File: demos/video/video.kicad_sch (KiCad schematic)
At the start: 5 parts, among them J4 DB9FEM, P1 BNC, P2 BNC, P3 BNC, P8 BNC

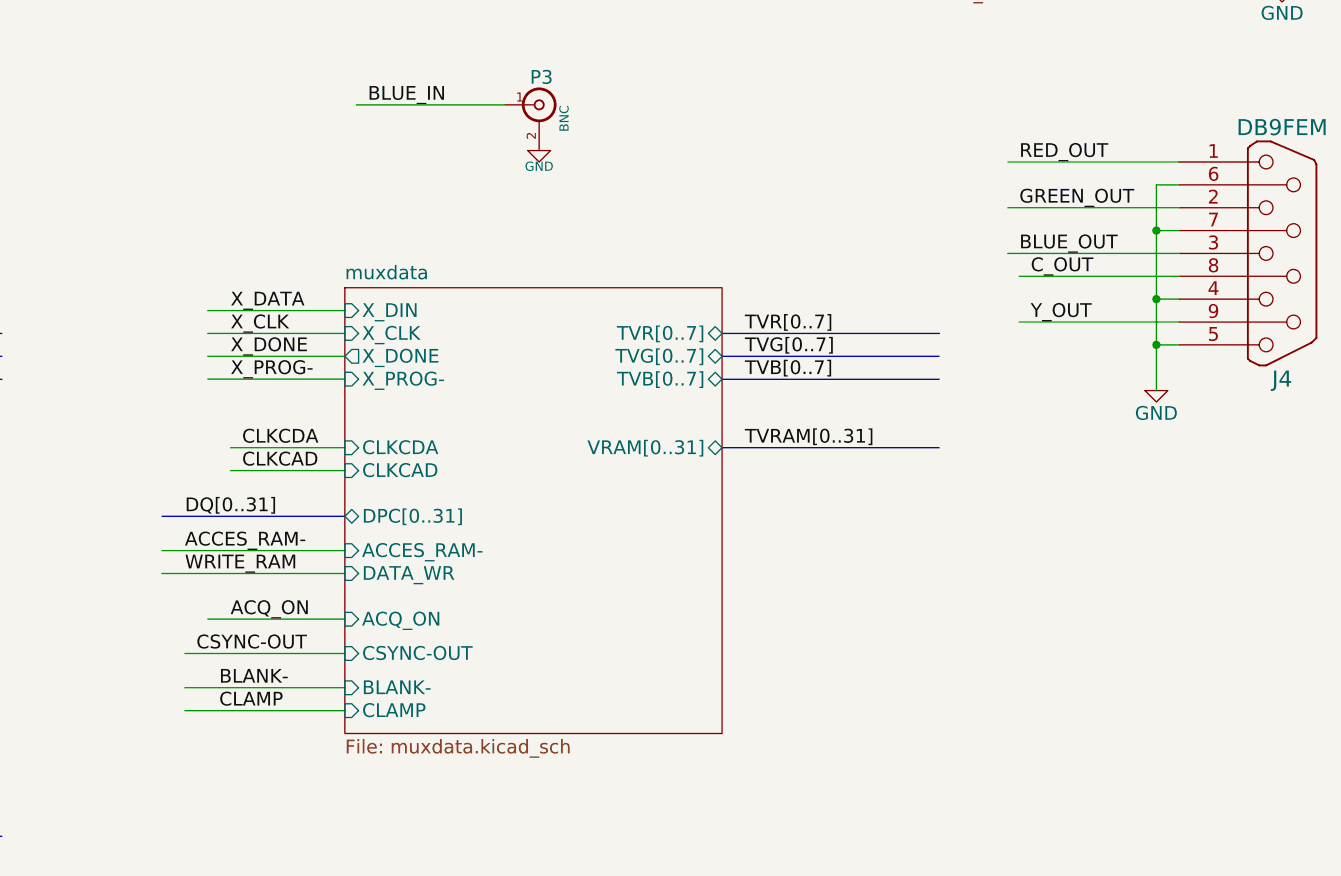
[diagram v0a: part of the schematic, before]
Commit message: feat: update kicad to 9.0.0+dfsg-1
Signed-off-by: lhdjply <lhdjply@126.com>
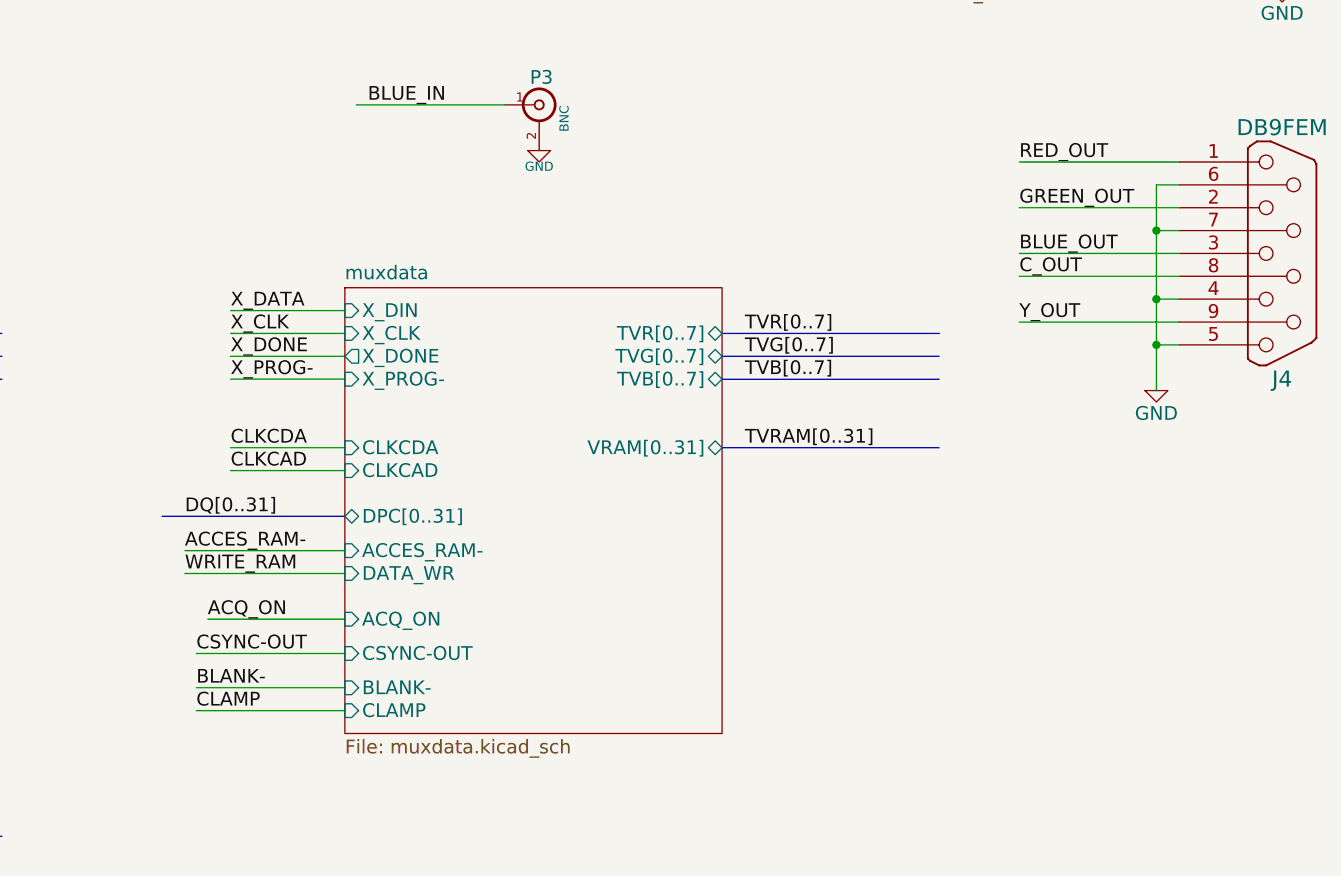
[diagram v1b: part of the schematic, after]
